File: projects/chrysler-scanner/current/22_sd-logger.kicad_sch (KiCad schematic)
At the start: 18 parts, among them J4 microSD / DM3AT-SF-PEJM5, SW3 LOG / SAFE STOP, U20 MCP1825S-3302E/DB

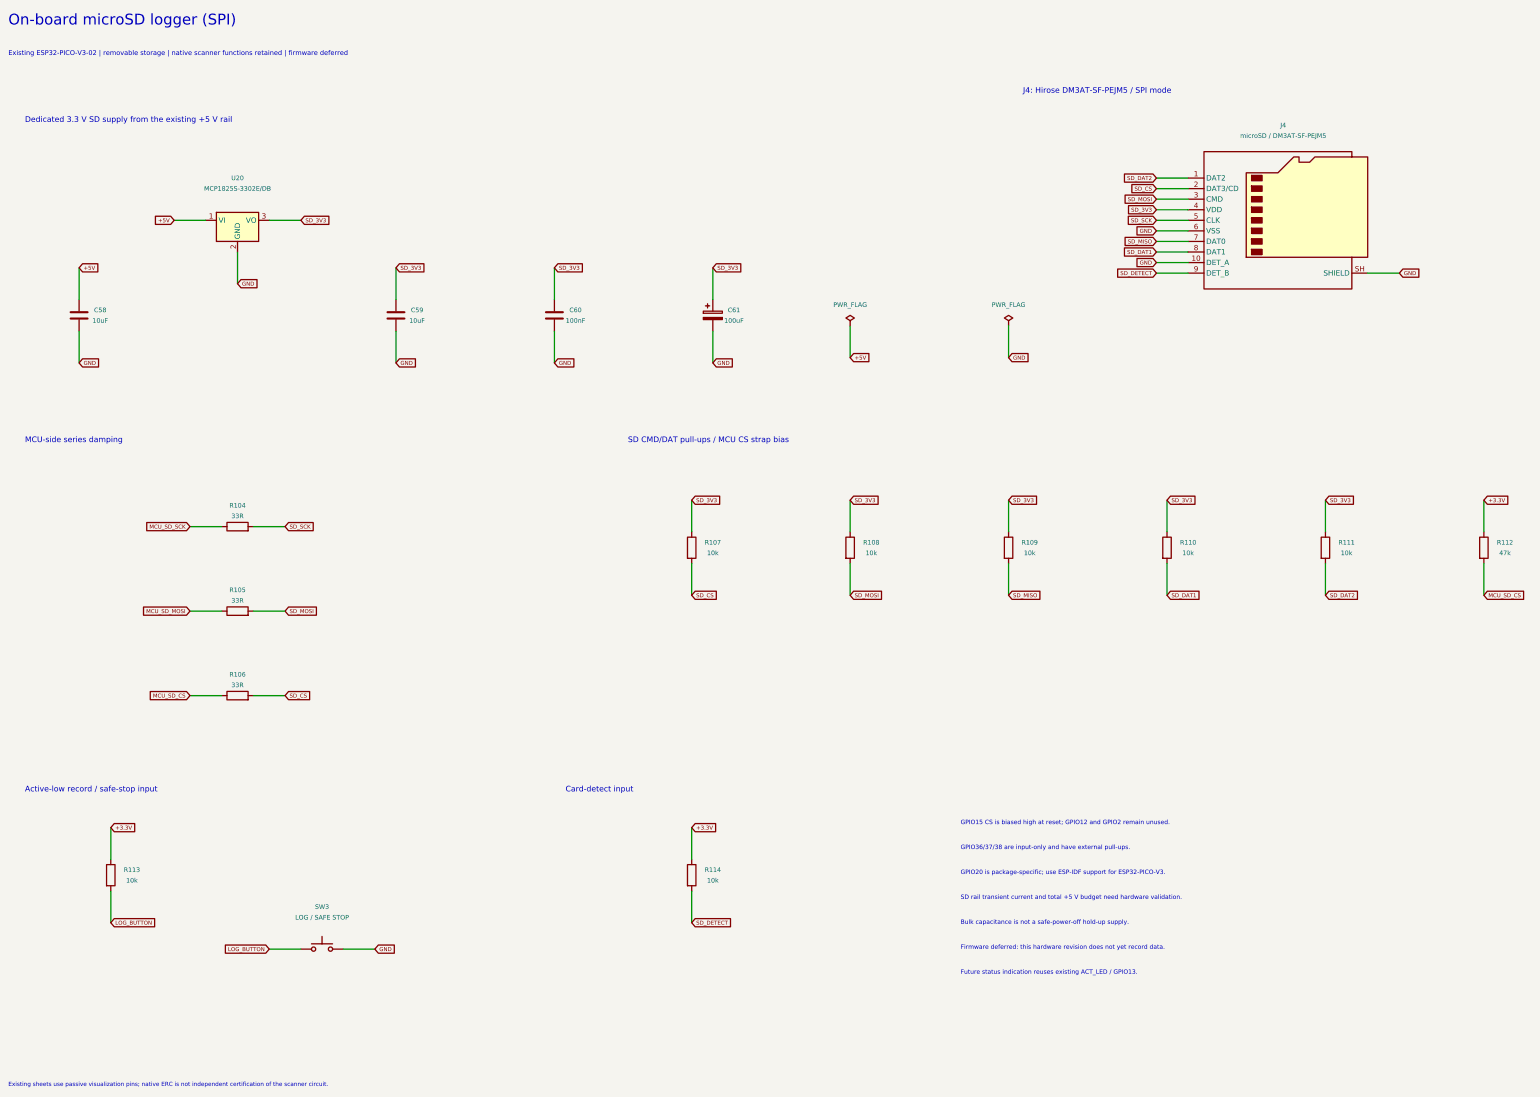
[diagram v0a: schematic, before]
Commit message: Finish scanner routing and add hierarchical system schematics
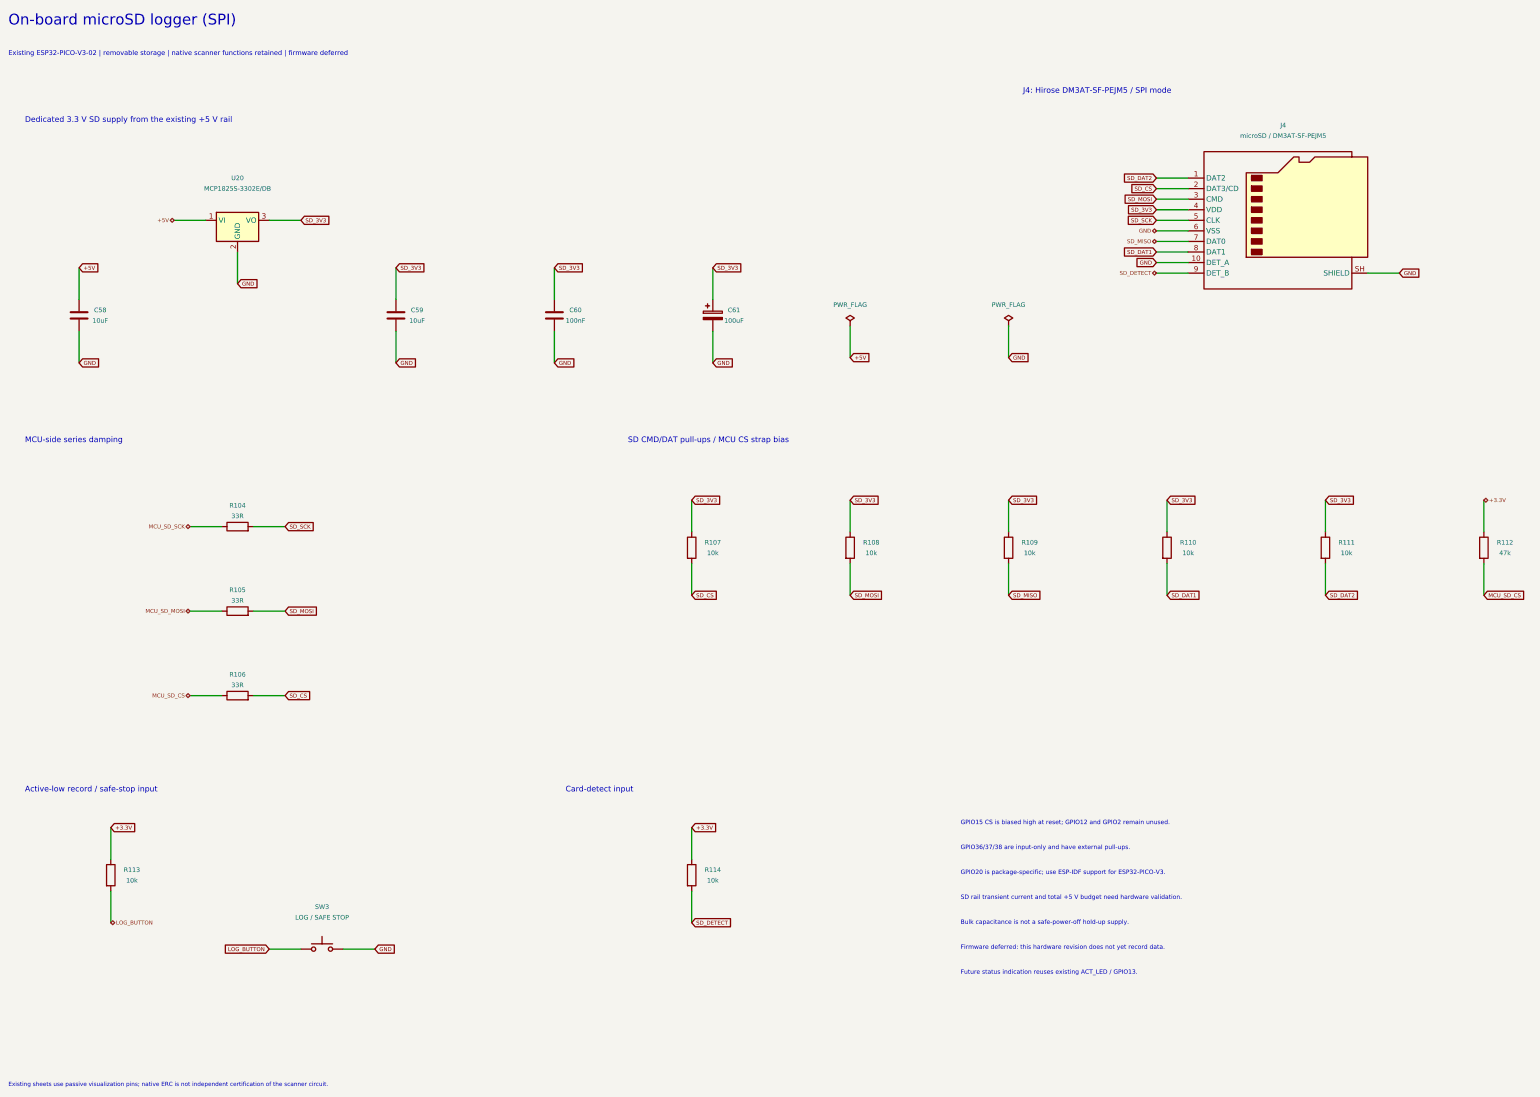
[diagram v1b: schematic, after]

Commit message: Use native ground symbols and document companion app feasibility
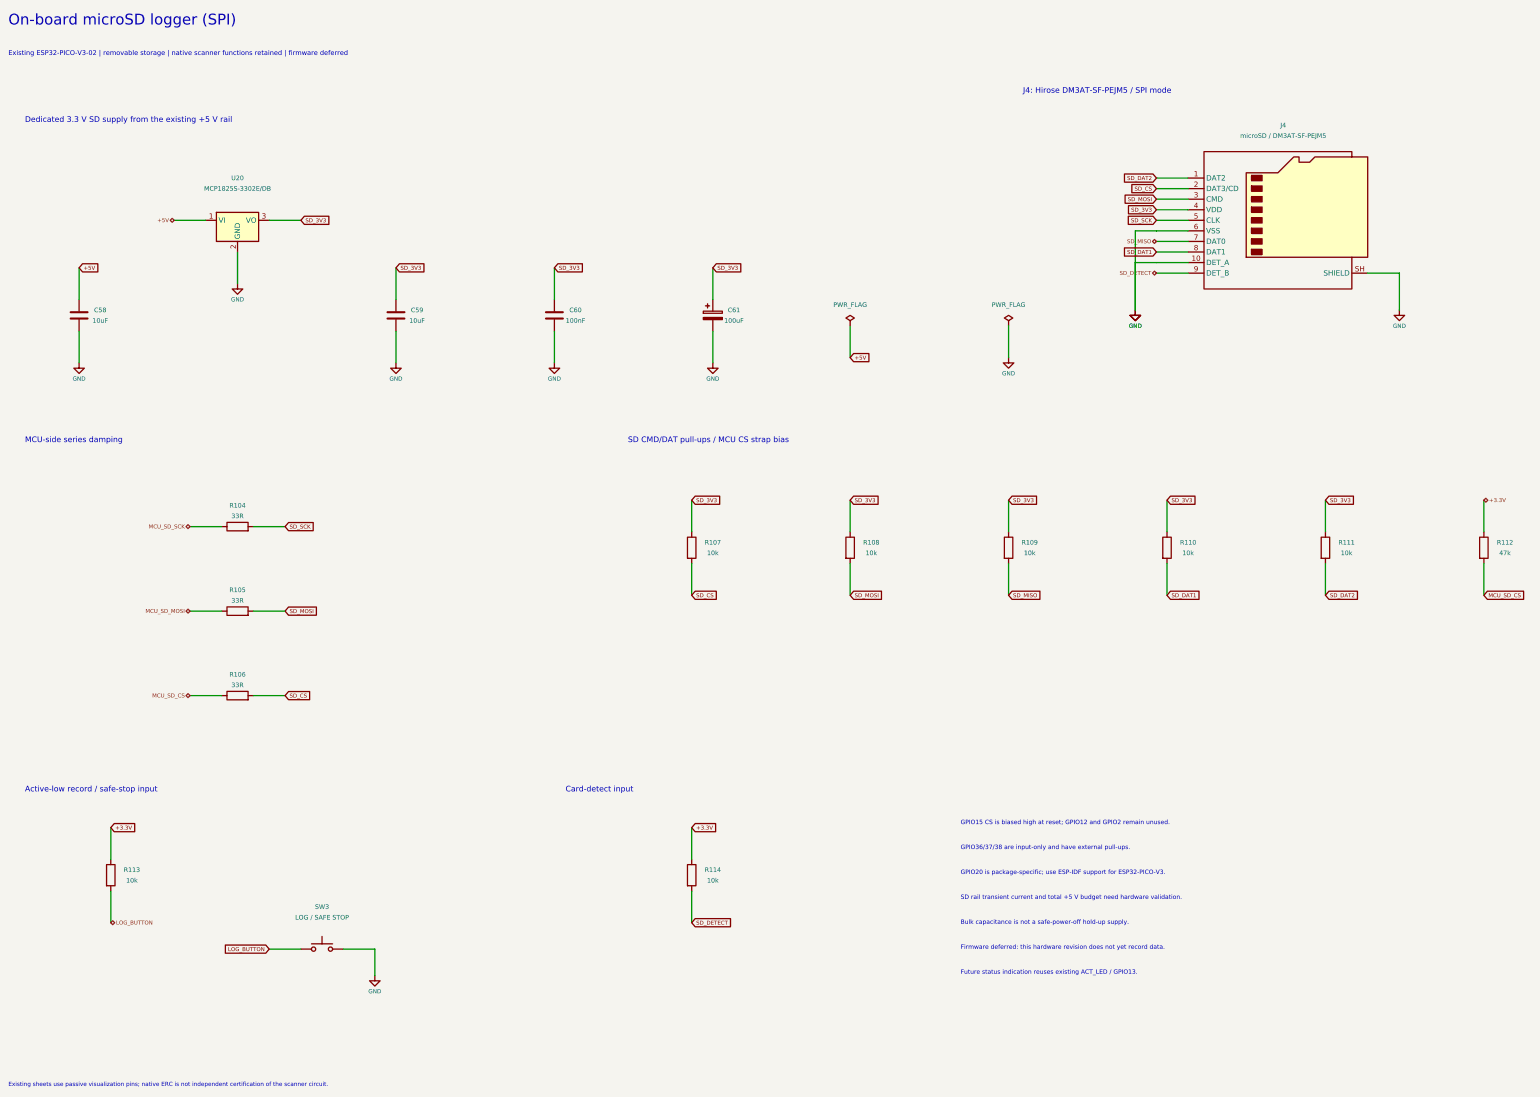
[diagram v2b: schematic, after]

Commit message: Fix scanner protection, ADC isolation and health watchdog
Coordinate the bounded 12 V input clamp and programming FET/capacitor ratings, add powered-off ADC isolation, and supervise the AW9523B permit with a dedicated GPIO13 health heartbeat. Preserve original placements and document all deliberate source-PDF deviations.

Validation: native ERC and full DRC/parity/refill report zero findings; strict preservation/connectivity audit and final adversarial review pass within the documented prototype bounds. Regenerate Rev C PDF, BOM, manufacturing exports, processing sites and verified portable archives. Compatible firmware and bench/mechanical qualification remain required.
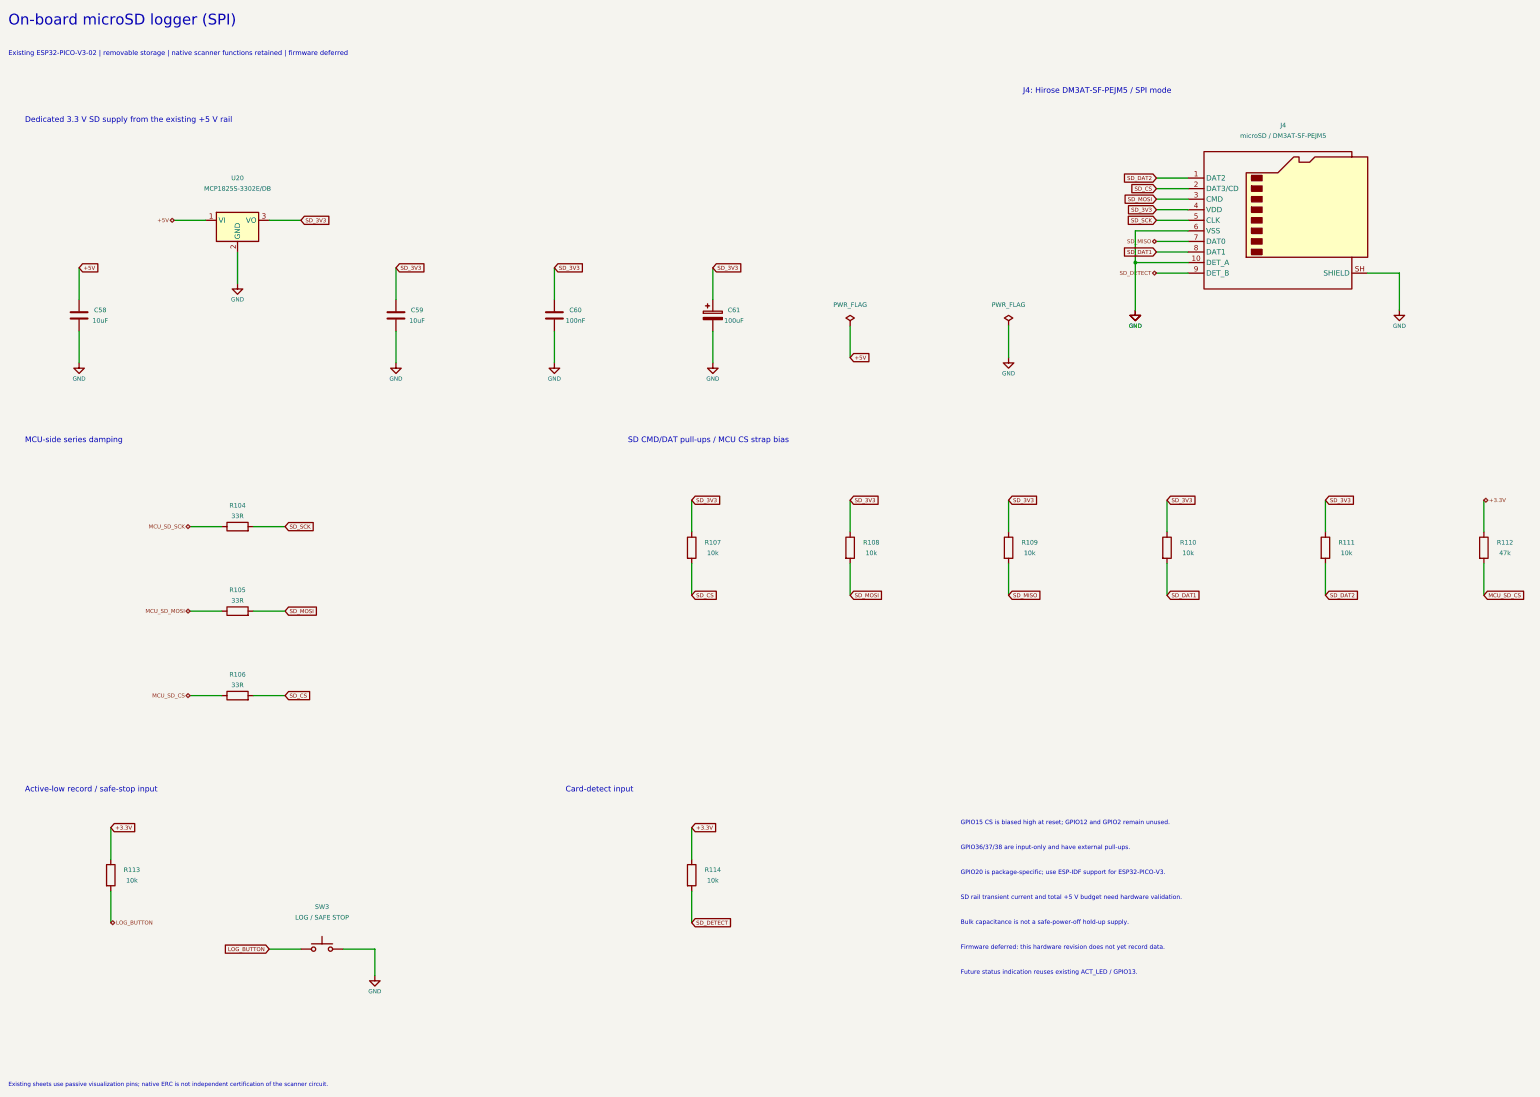
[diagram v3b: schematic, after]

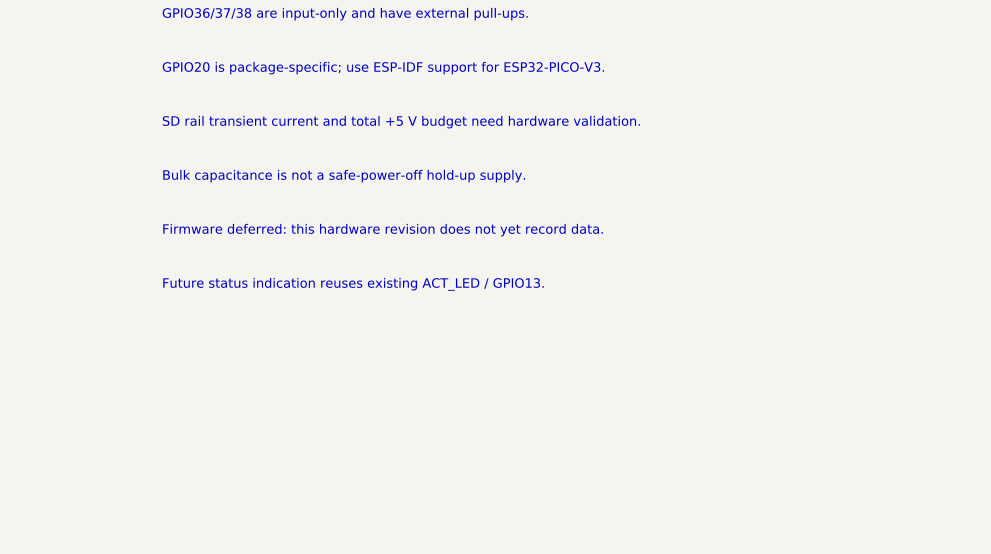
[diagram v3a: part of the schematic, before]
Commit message: Finish Chrysler scanner CCD correction and procurement fabrication package
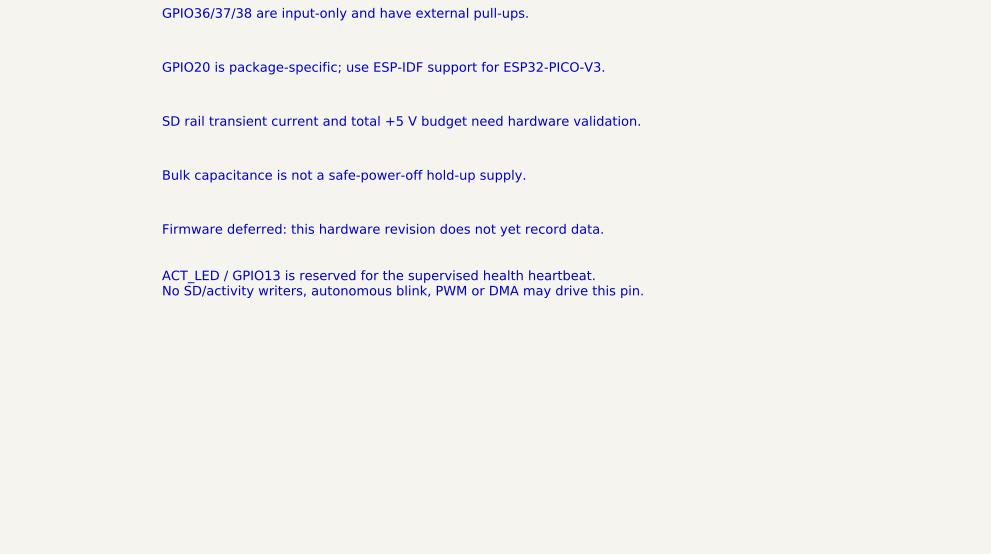
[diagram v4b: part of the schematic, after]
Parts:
- C58, C59: Assembly (none) -> PLACE; MPN GRM21BR71A106KE51L -> CGA4J1X5R1C106K125AC; Manufacturer Murata -> TDK; Procurement Source (none) -> https://product.tdk.com/info/en/documents/chara_sheet/CGA4J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; Selected Voltage Rating (none) -> 16V; Tolerance (none) -> 10%
- C60: Assembly (none) -> PLACE; MPN GRM188R71A104KA01D -> C0603C104K5RACTU; Manufacturer Murata -> KEMET; Procurement Source (none) -> https://search.kemet.com/component-documentation/download/s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; Selected Voltage Rating (none) -> 50V; Tolerance (none) -> 10%
- C61: Assembly (none) -> PLACE; Procurement Source (none) -> https://industrial.panasonic.com/ww/products/pt/os-con/mode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; Selected Voltage Rating (none) -> 6.3V; Tolerance (none) -> 20%
- J4: Assembly (none) -> PLACE; Procurement Source (none) -> https://www.hirose.com/product/p/CL0609-0031-0-00
- R104, R105, R106: Assembly (none) -> PLACE; MPN RC0603FR-0733RL -> CRCW060333R0FKEA; Manufacturer Yageo -> Vishay; Procurement Source (none) -> https://www.vishay.com/docs/20035/dcrcwe3.pdf; Selected Power Rating (none) -> 0.1W; Tolerance (none) -> 1%
- R107, R108, R109, R110, R111, R113, R114: Assembly (none) -> PLACE; MPN RC0603FR-0710KL -> CRCW060310K0FKEA; Manufacturer Yageo -> Vishay; Procurement Source (none) -> https://www.vishay.com/docs/20035/dcrcwe3.pdf; Selected Power Rating (none) -> 0.1W; Tolerance (none) -> 1%
- R112: Assembly (none) -> PLACE; MPN RC0603FR-0747KL -> CRCW060347K0FKEA; Manufacturer Yageo -> Vishay; Procurement Source (none) -> https://www.vishay.com/docs/20035/dcrcwe3.pdf; Selected Power Rating (none) -> 0.1W; Tolerance (none) -> 1%
- SW3: Assembly (none) -> PLACE; Procurement Source (none) -> https://www.e-switch.com/wp-content/uploads/2023/01/TL3305.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
- U20: Assembly (none) -> PLACE; Procurement Source (none) -> https://ww1.microchip.com/downloads/en/DeviceDoc/22056b.pdf
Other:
- note added: "ACT_LED / GPIO13 is reserved for the supervised health heartbeat. No SD/activity writers, autonomous blink, PWM or DMA may drive this pin."
- note removed: "Future status indication reuses existing ACT_LED / GPIO13."
